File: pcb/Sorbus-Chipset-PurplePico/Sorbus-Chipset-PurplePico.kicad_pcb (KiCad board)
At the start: 2 copper layers, 83.8 x 48.3 mm, 4 parts, among them J1 Conn_01x32_Pin, J2 Conn_01x20_Pin, J3 Conn_01x20_Pin, J4 Conn_01x05_Pin

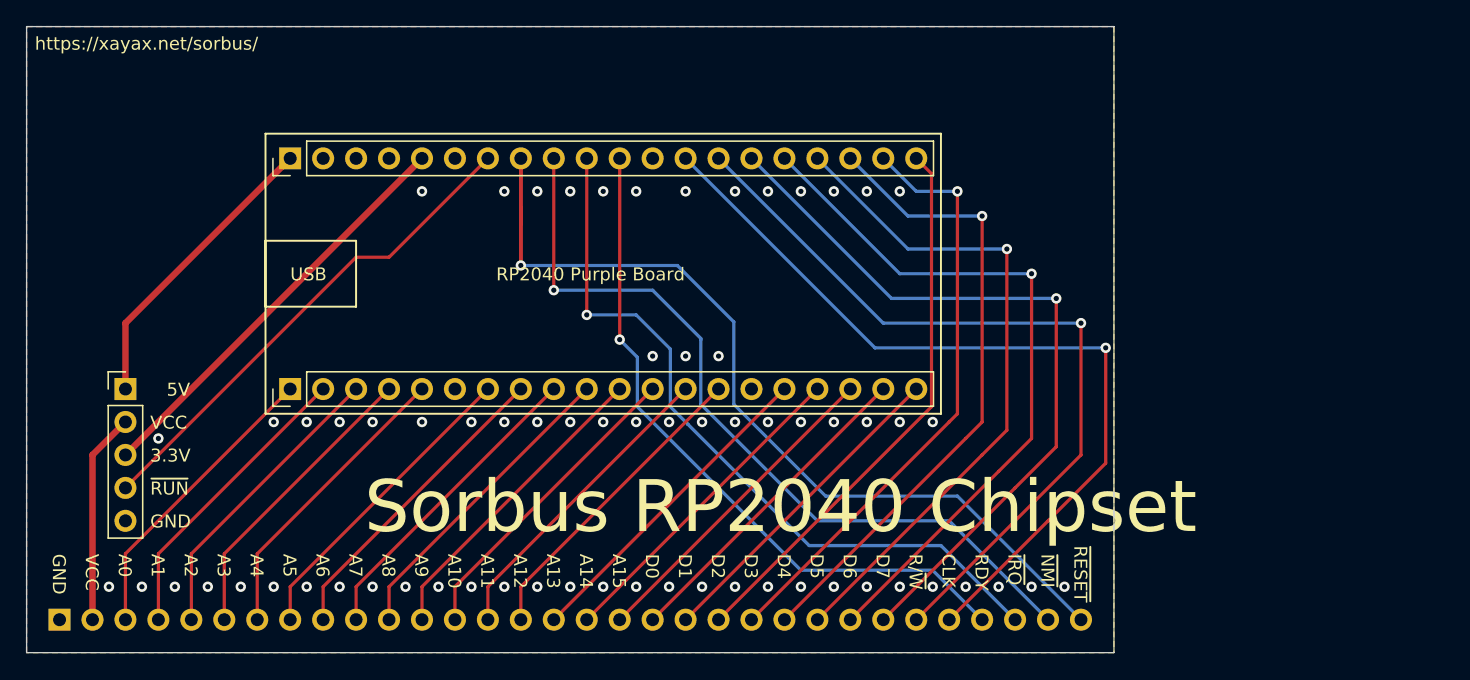
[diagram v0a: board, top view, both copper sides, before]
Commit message: updated PCB design - added decoupling capacitor to 65C02 board - replaced simple connectors with real RP2040 Purple component - also updated gerber file and PDF exports from PCB changes - fixed problem in bare build
Signed-off-by: Sven Oliver Moll <svolli@svolli.de>
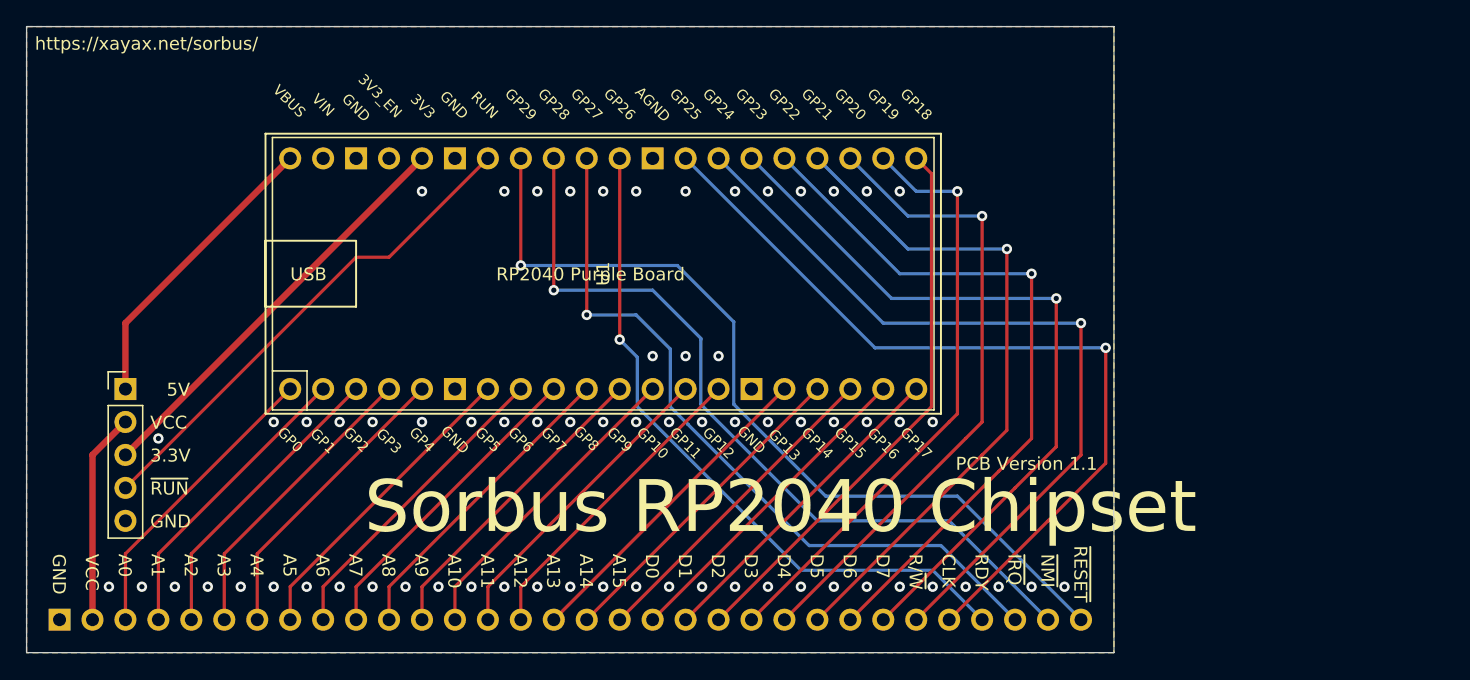
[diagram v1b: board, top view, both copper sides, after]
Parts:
- removed the J2 at (45.7, 45.7)
- removed J3: Conn_01x20_Pin, Connector_PinHeader_2.54mm:PinHeader_1x20_P2.54mm_Vertical
- added U1: PurpleRP2040_no_debug, MCU_RaspberryPi_and_Boards:RPi_RP2040Purple_SMD_TH_no_debug, F.Cu at (69.8, 36.8)
- renumbered J4 to J2
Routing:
- net ~{RESET}: track 76.0 -> 66.5 mm
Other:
- board text added: "PCB Version 1.1"
